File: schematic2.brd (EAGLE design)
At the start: 101.6 x 53.3 mm, 71 parts, among them IC6 DS3231/SO

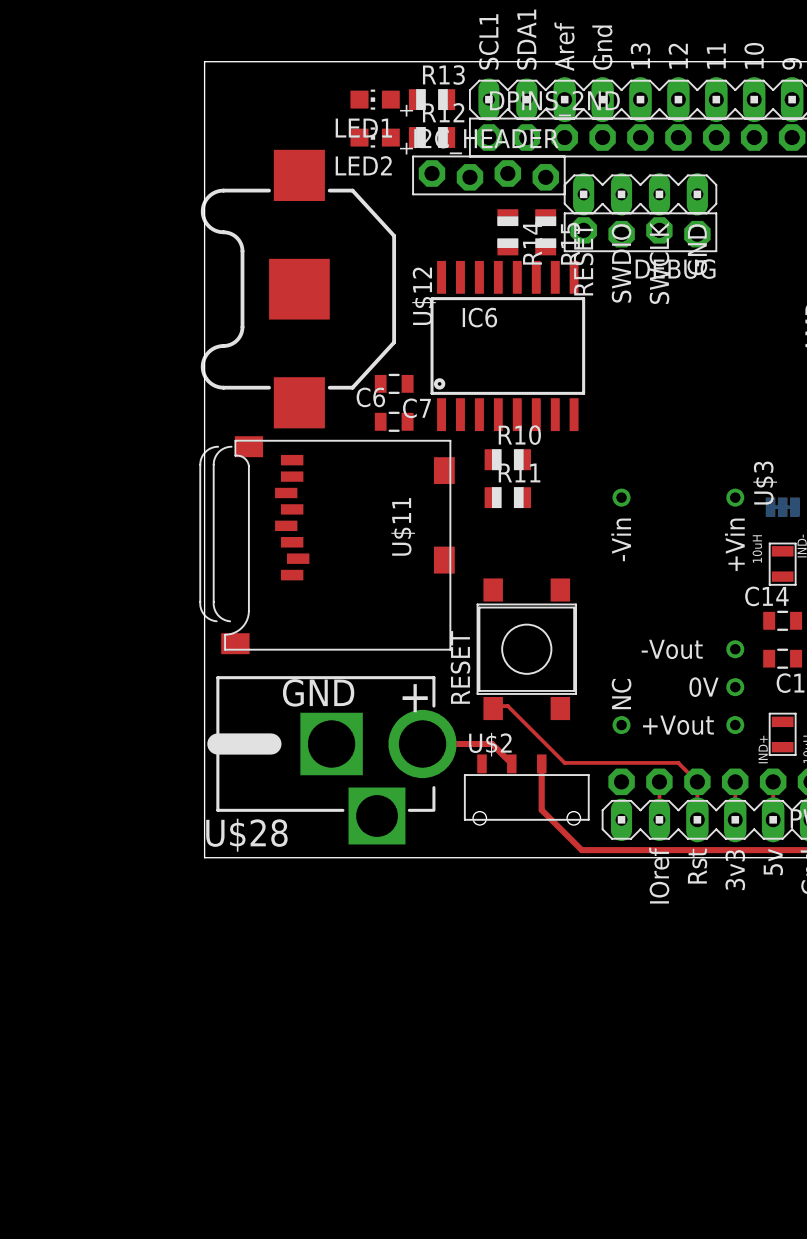
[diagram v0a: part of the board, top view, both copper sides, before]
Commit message: Fixed the RC filter arrangement on the 2nd stage op-amps for all three inputs. Move the adjust resistors (for 2nd stage amplification setting) in line with the signal line from the AD620s to the LM324s.
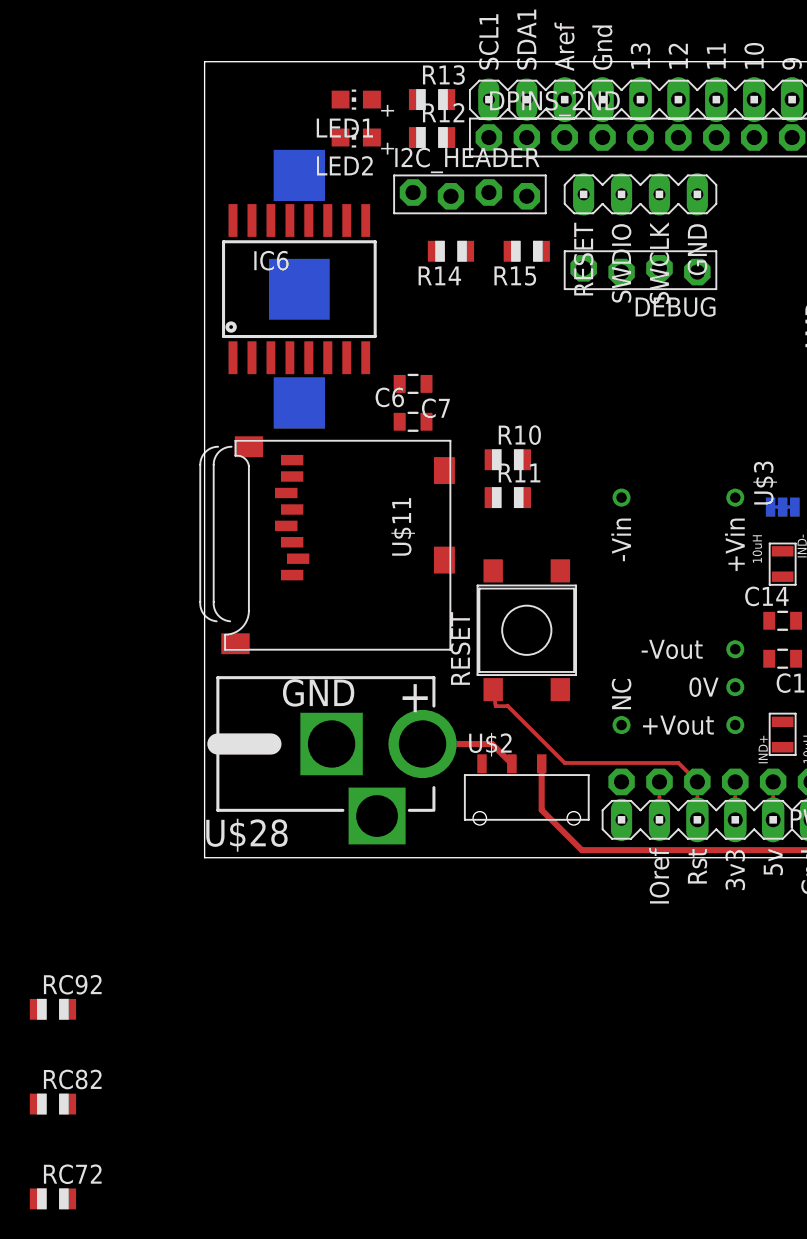
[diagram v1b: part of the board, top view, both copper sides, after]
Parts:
- added RC72, RC82, RC92: 33k ohm, Felicia_force_logger:R0805
- C72, C82, C92: value (none) -> 3.3nF
- moved IC6 14.5 mm to (6.35, 38.1)
- moved R14 4.02 mm to (16.5, 40.6), turned to 180 degrees
- moved DEBUG 2.54 mm to (29.2, 39.4)
- moved I2C_HEADER 1.80 mm to (17.8, 44.5)
- moved R15 1.80 mm to (21.6, 40.6), turned to 180 degrees
- moved C6 1.27 mm to (14.0, 29.2)
- moved C7 1.27 mm to (14.0, 31.8)
- moved LED1 1.27 mm to (10.2, 50.8)
- moved LED2 1.27 mm to (10.2, 48.3)
- moved RESET 1.27 mm to (21.6, 15.2)
- flipped U$12 to the bottom, turned to 270 degrees
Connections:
- removed net N$26: IC6.14, U$12.P$1
- new net N$3: JOY_X.6, R$80.1
- new net N$4: BEAM_Z.6, R$70.1
- new net N$8: JOY_Y.6, R$90.1
- new net VBAT: IC6.14, U$12.P$1, U$12.P$2
- net A0: now also RC82.1; no longer R$80.2
- net A1: now also RC92.1; no longer R$90.2
- net A2: now also RC72.1; no longer R$70.2
- net N$11: now also R$80.2, RC82.2; no longer JOY_X.6, R$80.1
- net N$21: now also R$90.2, RC92.2; no longer JOY_Y.6, R$90.1
- net N$25: now also R$70.2, RC72.2; no longer BEAM_Z.6, R$70.1
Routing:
- net RESET: track 18.4 -> 19.3 mm

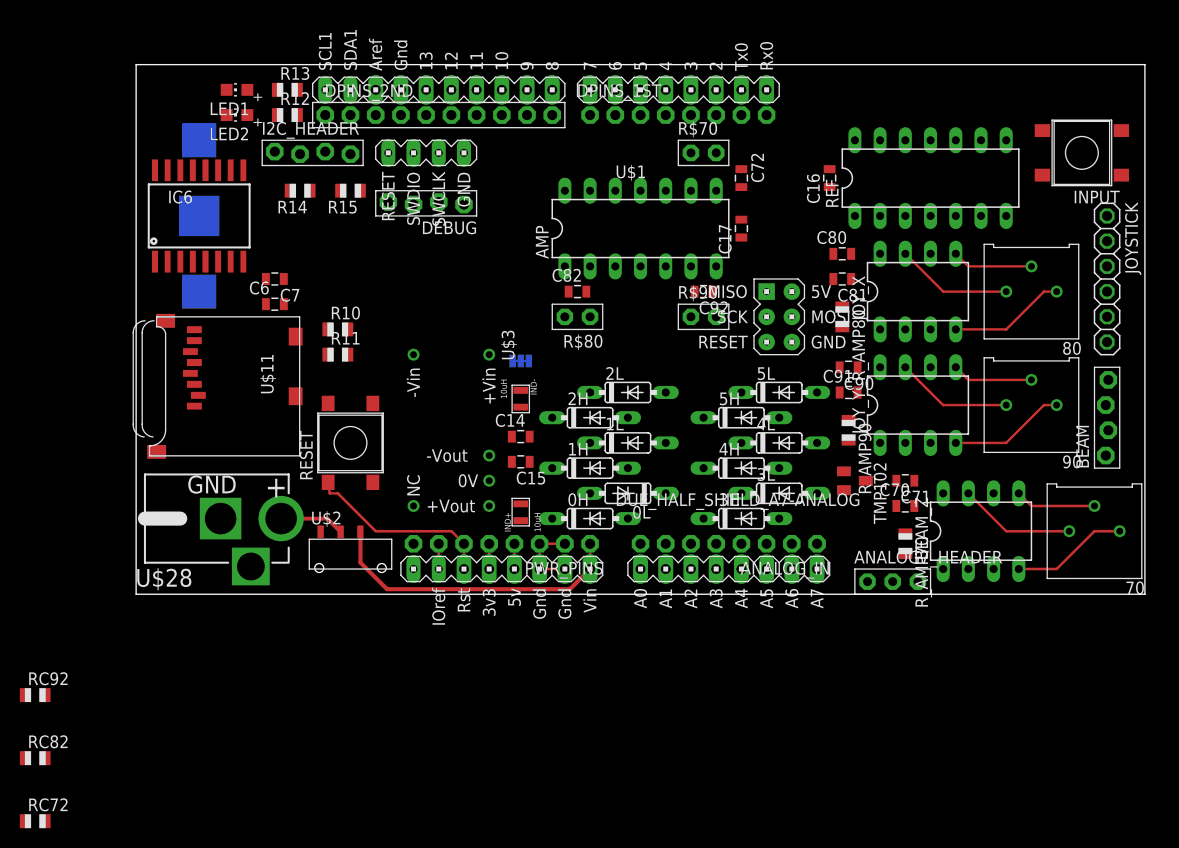
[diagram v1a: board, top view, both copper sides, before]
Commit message: Moved the amps around to try to minimize the rats nest. Moved all capacitors to the underside of the board, while all resistors and inductors remain on the top of the board. Added two mounting holes just for the hell of it.
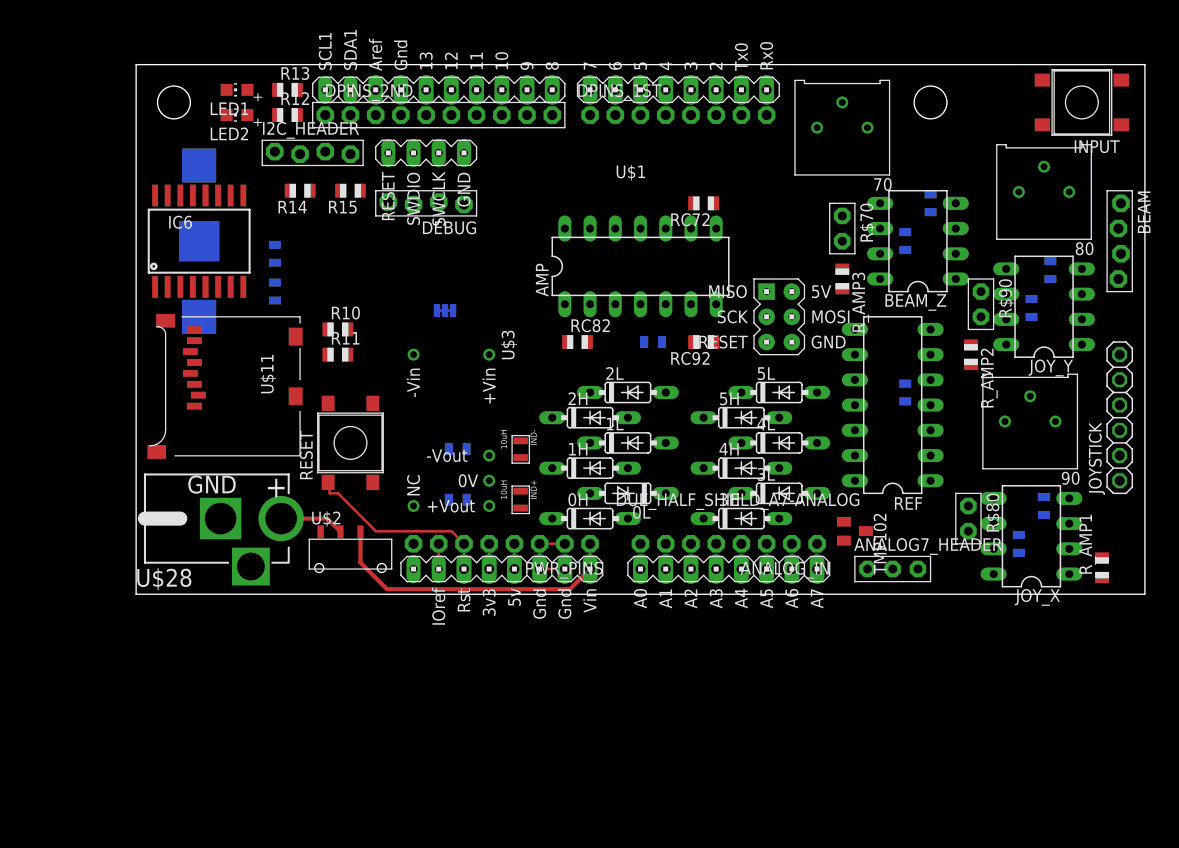
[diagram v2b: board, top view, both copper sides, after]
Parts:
- removed R_AMP70, R_AMP80, R_AMP90: 10K, Felicia_force_logger:R0805
- added R_AMP1, R_AMP2, R_AMP3: 10K, Felicia_force_logger:R0805
- added STANDOFF1, STANDOFF2: STAND-OFF, miller:STAND-OFF
- moved RC72 91.7 mm to (57.1, 39.4), turned to 180 degrees
- moved RC92 76.1 mm to (57.1, 25.4), turned to 180 degrees
- moved RC82 68.8 mm to (44.5, 25.4)
- moved 70 47.9 mm to (71.1, 47.0)
- moved R$80 44.3 mm to (83.8, 7.62), turned to 270 degrees
- moved C80 34.2 mm to (88.9, 5.08), flipped to the bottom, turned to 90 degrees
- moved C81 30.6 mm to (91.4, 8.89), flipped to the bottom, turned to 270 degrees
- moved BEAM_Z 29.9 mm to (78.7, 35.6), turned to 90 degrees
- moved C71 28.1 mm to (80.0, 39.4), flipped to the bottom, turned to 270 degrees
- moved R$90 28.0 mm to (85.1, 29.2), turned to 270 degrees
- moved JOY_X 27.2 mm to (90.2, 5.84), turned to 90 degrees
- moved C70 26.7 mm to (77.5, 35.6), flipped to the bottom, turned to 270 degrees
- moved C91 23.8 mm to (92.1, 32.6), flipped to the bottom, turned to 90 degrees
- moved REF 23.2 mm to (76.2, 19.1), turned to 90 degrees
- moved C16 22.9 mm to (77.5, 20.3), flipped to the bottom, turned to 270 degrees
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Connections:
- net N$10: now also R_AMP3.1; no longer R_AMP70.1
- net N$2: now also R_AMP2.2; no longer R_AMP90.2
- net N$5: now also R_AMP1.2; no longer R_AMP80.2
- net N$6: now also R_AMP1.1; no longer R_AMP80.1
- net N$7: now also R_AMP2.1; no longer R_AMP90.1
- net N$9: now also R_AMP3.2; no longer R_AMP70.2
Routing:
- net +5V: track 35.2 -> 0.00 mm
- net VNEG: track 35.2 -> 0.00 mm
- net A4: track 8.15 -> 0.00 mm
- net A3: track 8.15 -> 0.00 mm
- net A5: track 8.15 -> 0.00 mm

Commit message: Started routing the analog lines, and some of the digital lines.
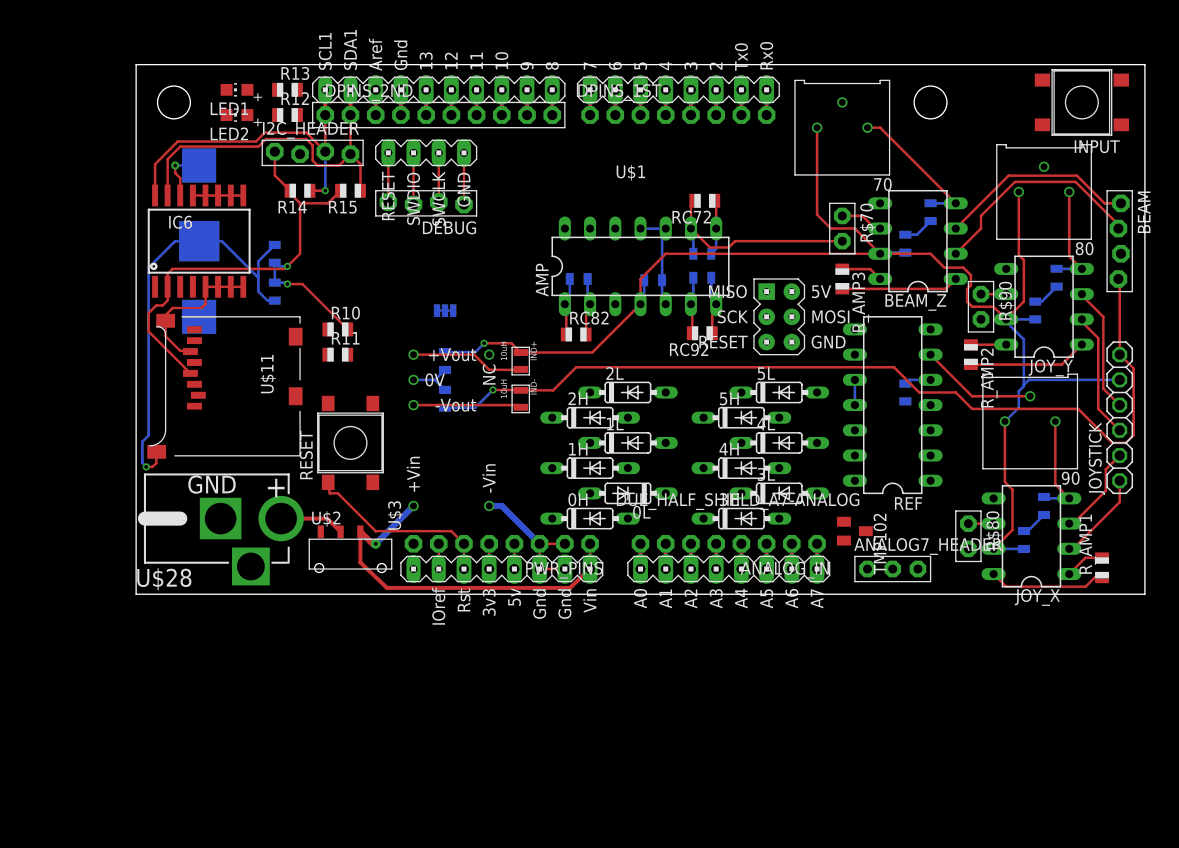
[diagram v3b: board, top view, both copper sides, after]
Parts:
- moved C15 14.0 mm to (31.1, 23.5), turned to 90 degrees
- moved IND+ 14.0 mm to (38.7, 23.5)
- moved C92 6.48 mm to (57.0, 31.9)
- moved C82 6.35 mm to (44.6, 31.8)
- moved C17 6.22 mm to (52.1, 31.6)
- moved C14 5.24 mm to (31.1, 19.7), turned to 90 degrees
- moved C72 5.08 mm to (57.0, 34.3)
- moved IND- 5.08 mm to (38.7, 19.7)
- moved R$80 1.78 mm to (83.8, 5.84)
- moved C91 0.99 mm to (92.7, 31.9), turned to 270 degrees
- moved RC92 0.90 mm to (57.0, 26.3)
- moved C71 0.89 mm to (80.0, 38.5)
- moved RC82 0.77 mm to (44.3, 26.2)
- moved C80 0.63 mm to (89.4, 5.46), turned to 270 degrees
- moved C90 0.46 mm to (90.6, 28.6), turned to 270 degrees
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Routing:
- net +5V: track 0.00 -> 145.0 mm, vias 0 -> 1
- net -5V: track 0.00 -> 90.9 mm, vias 0 -> 1
- net DGND: track 0.00 -> 64.3 mm, vias 0 -> 1
- net +3V3: track 2.54 -> 58.3 mm, vias 0 -> 2
- net VNEG: track 0.00 -> 36.3 mm
- net SDA1: track 0.00 -> 36.0 mm
- net SCL1: track 0.00 -> 34.1 mm, vias 0 -> 1
- net AGND: track 0.00 -> 24.3 mm
- net N$31: track 0.00 -> 22.3 mm
- net N$25: track 0.00 -> 21.9 mm
- net N$32: track 0.00 -> 20.0 mm
- net A4: track 0.00 -> 14.3 mm
- net GND: track 7.62 -> 21.8 mm
- net N$24: track 0.00 -> 12.8 mm
- net N$23: track 0.00 -> 12.8 mm
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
